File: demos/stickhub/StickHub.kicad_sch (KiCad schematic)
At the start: 94 parts, among them J1 HOST, J2 USB1, J3 USB2, J4 USB3, J5 USB4, J6 USB5, J7 USB6, J8 USB7, J9 EXTGND, U1 MaxLinear_XR22417-48, U2 Dialog_SLG5NT1487V, Y1 12MHz 50ppm 16-20pF

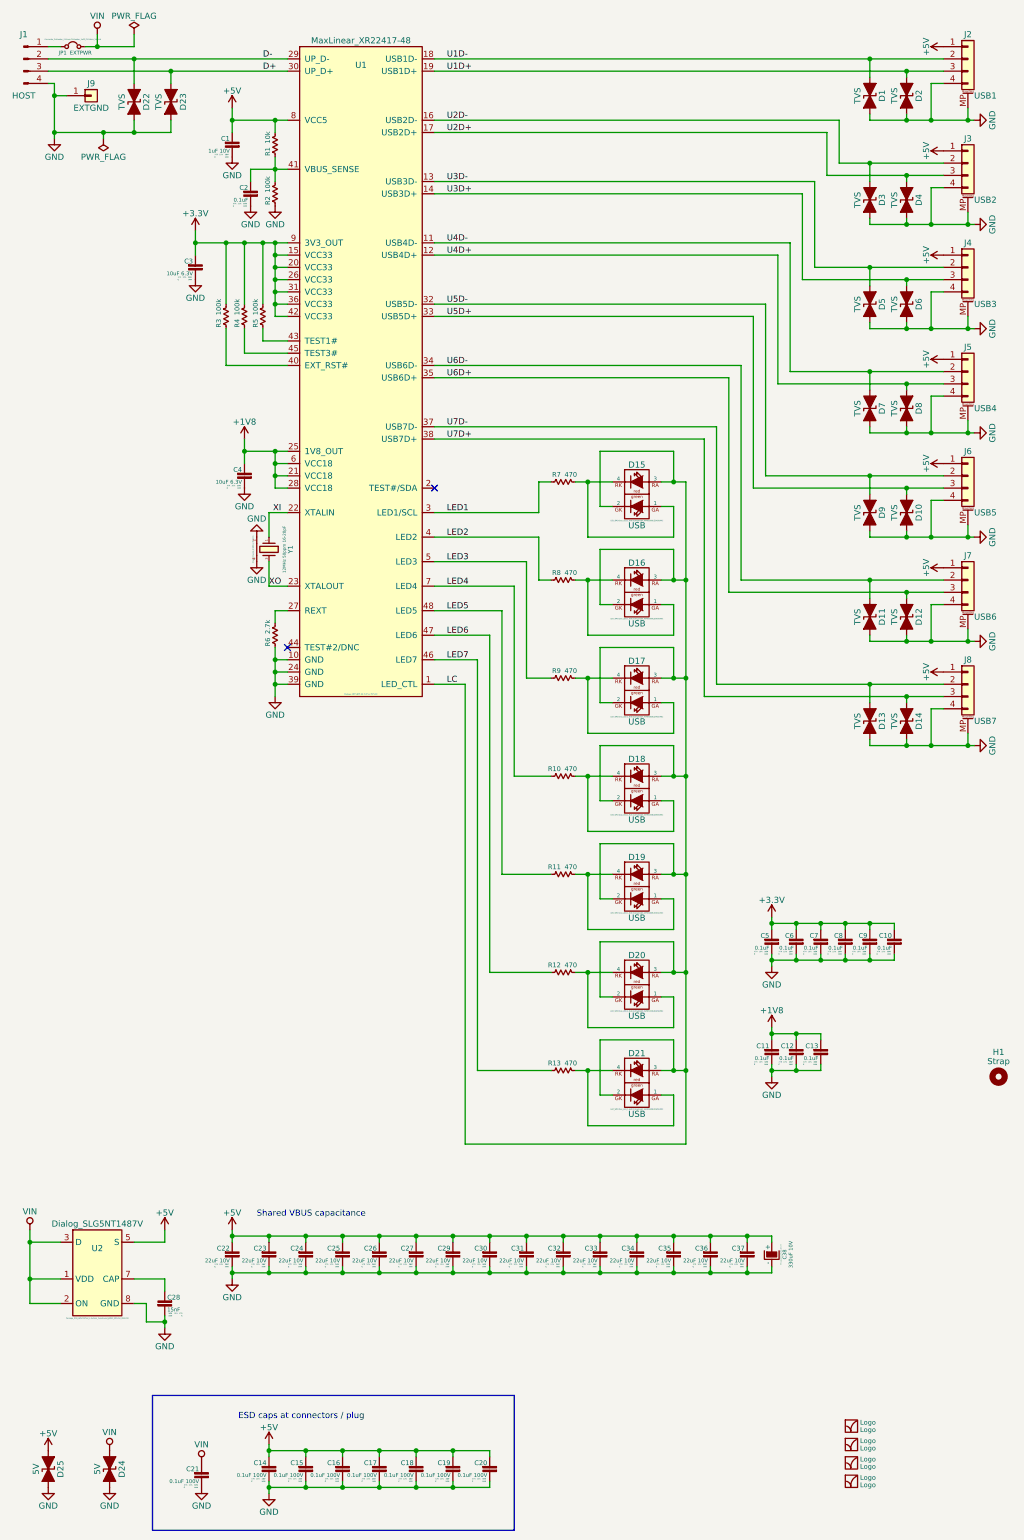
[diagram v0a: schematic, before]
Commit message: feat: update kicad to 9.0.0+dfsg-1
Signed-off-by: lhdjply <lhdjply@126.com>
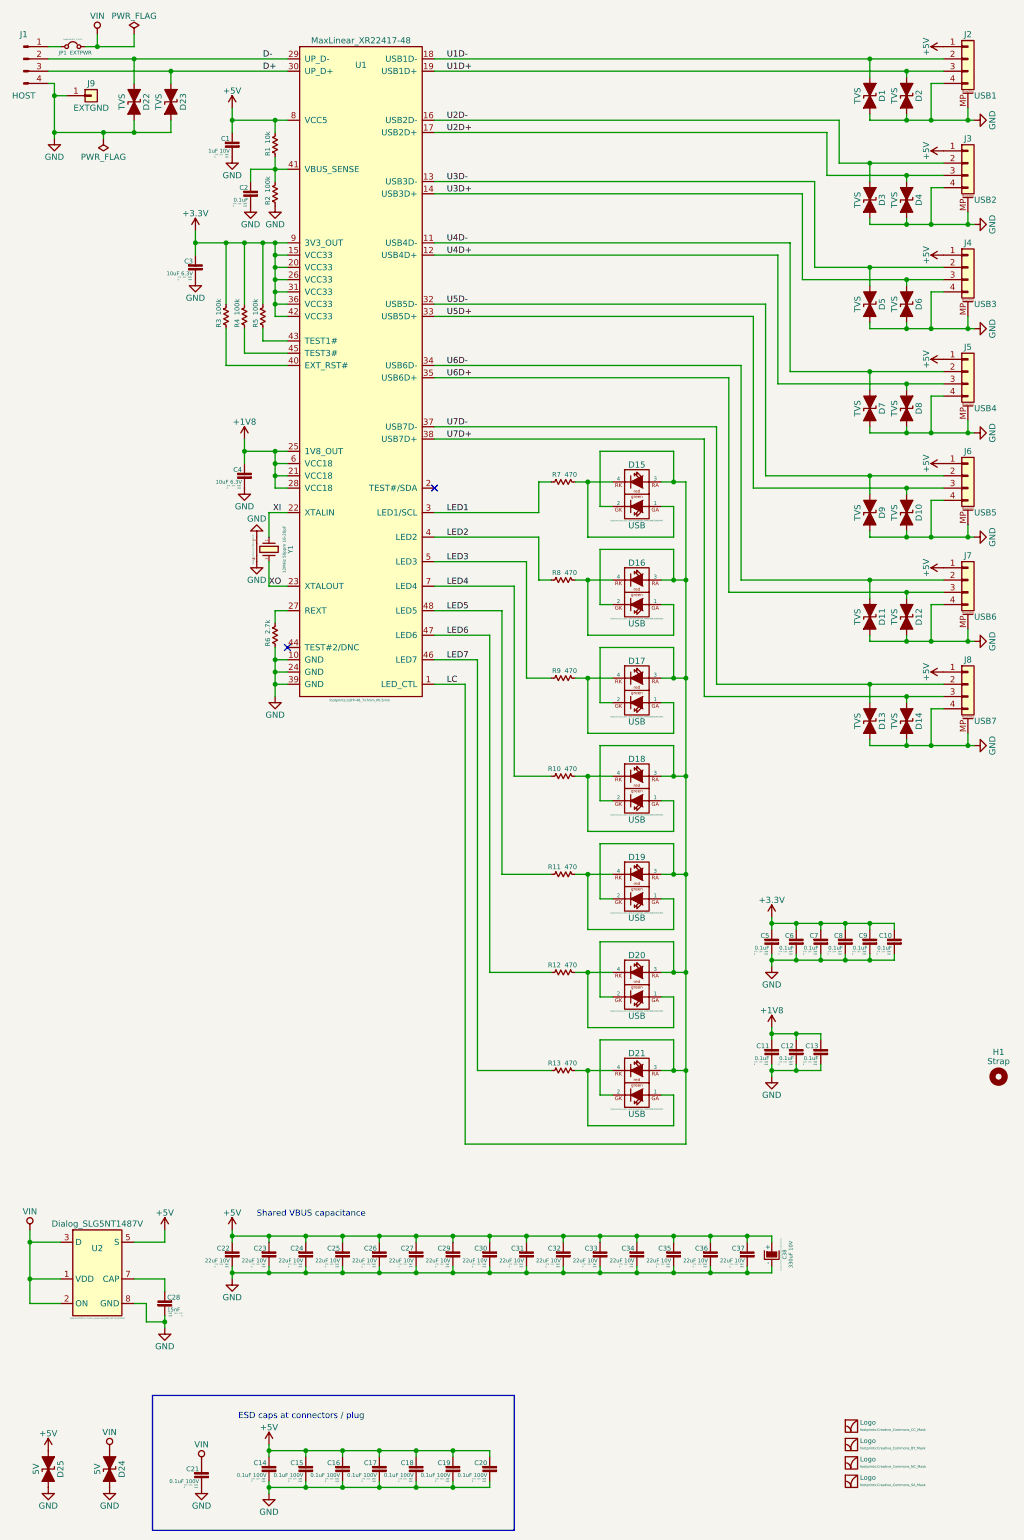
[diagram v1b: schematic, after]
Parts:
- C1, C10, C11, C12, C13, C2, C28, C3, C4, C5, C6, C7, C8, C9: footprint Capacitor_SMD:1608_C -> footprints:1005_C
- C14, C15, C16, C17, C18, C19, C20, C21: footprint Capacitor_SMD:1608_C -> footprints:2012_C
- C22, C23, C24, C25, C26, C27, C29, C30, C31, C32, C33, C34, C35, C36, C37: footprint Capacitor_SMD:1608_C -> footprints:1608_C
- C38: footprint SH_Capacitors:CP_Elec_6.3x7.7 -> footprints:CP_Elec_6.3x11_Board_Edge_Mirrored
- D1, D10, D11, D12, D13, D14, D2, D22, D23, D24, D25, D3, D4, D5, D6, D7, D8, D9: footprint Diode_SMD:1006_C -> footprints:D_0402
- D15, D16, D17, D18, D19, D20, D21: footprint LED_SMD:Duo_LED_1.6x0.8_Kingbright_APHB1608LZGKSURKC -> footprints:Duo_LED_1.6x0.8_Kingbright_APHB1608LZGKSURKC
- H1: footprint MountingHole:Plain_Hole_3mm -> footprints:Plain_Hole_3mm
- J1: footprint Connector_USB:USB_A_PCB_traces_small -> footprints:USB_A_PCB_traces_small
- J2, J3, J4, J5, J6, J7, J8: footprint Connector_JST:JST_SH_SM04B-SRSS-TB_1x04-1MP_P1.00mm_Horizontal -> footprints:JST_SH_SM04B-SRSS-TB_1x04-1MP_P1.00mm_Horizontal
- J9: footprint SH_Solder_Pads:1P-1.5x1.5 -> footprints:1P-1.5x1.5
- JP1: footprint Connector_PinHeader_2.54mm:PinHeader_1x02_P2.54mm_Vertical -> footprints:JP-2_1.5x1.5
- LOGO1: footprint Logo -> footprints:Creative_Commons_CC_Mask
- LOGO2: footprint Logo -> footprints:Creative_Commons_BY_Mask
- LOGO3: footprint Logo -> footprints:Creative_Commons_NC_Mask; symbol RobotProtos:Logo -> RobotProtos:Logo_2
- LOGO4: footprint Logo -> footprints:Creative_Commons_SA_Mask; symbol RobotProtos:Logo -> RobotProtos:Logo_3
- R1, R10, R11, R12, R13, R2, R3, R4, R5, R6, R7, R8, R9: footprint Resistor_SMD:1608_C -> footprints:R_1005_C
- U1: footprint Package_QFP:LQFP-48_7x7mm_P0.5mm -> footprints:LQFP-48_7x7mm_P0.5mm
- U2: footprint Package_DFN_QFN:TDFN-8_1.5x2mm_Fused-Lead_JEDEC_MO-252_W2015D -> footprints:TDFN-8_1.5x2mm_Fused-Lead_JEDEC_MO-252_W2015D
- Y1: footprint Crystal:Crystal_4-SMD_2.5x2mm -> footprints:Crystal_4-SMD_2.5x2mm
